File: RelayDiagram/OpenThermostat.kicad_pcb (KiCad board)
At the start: 2 copper layers, 9 parts, among them J1 Barrel_Jack_Switch, J2 Conn_01x15_Female, J3 Conn_01x15_Female, J4 Conn_01x08_Female, J5 Conn_01x11_Female, U1 R-78E3.3-1.0, U2 34.81-9024, U3 34.81-9024, U4 34.81-9024

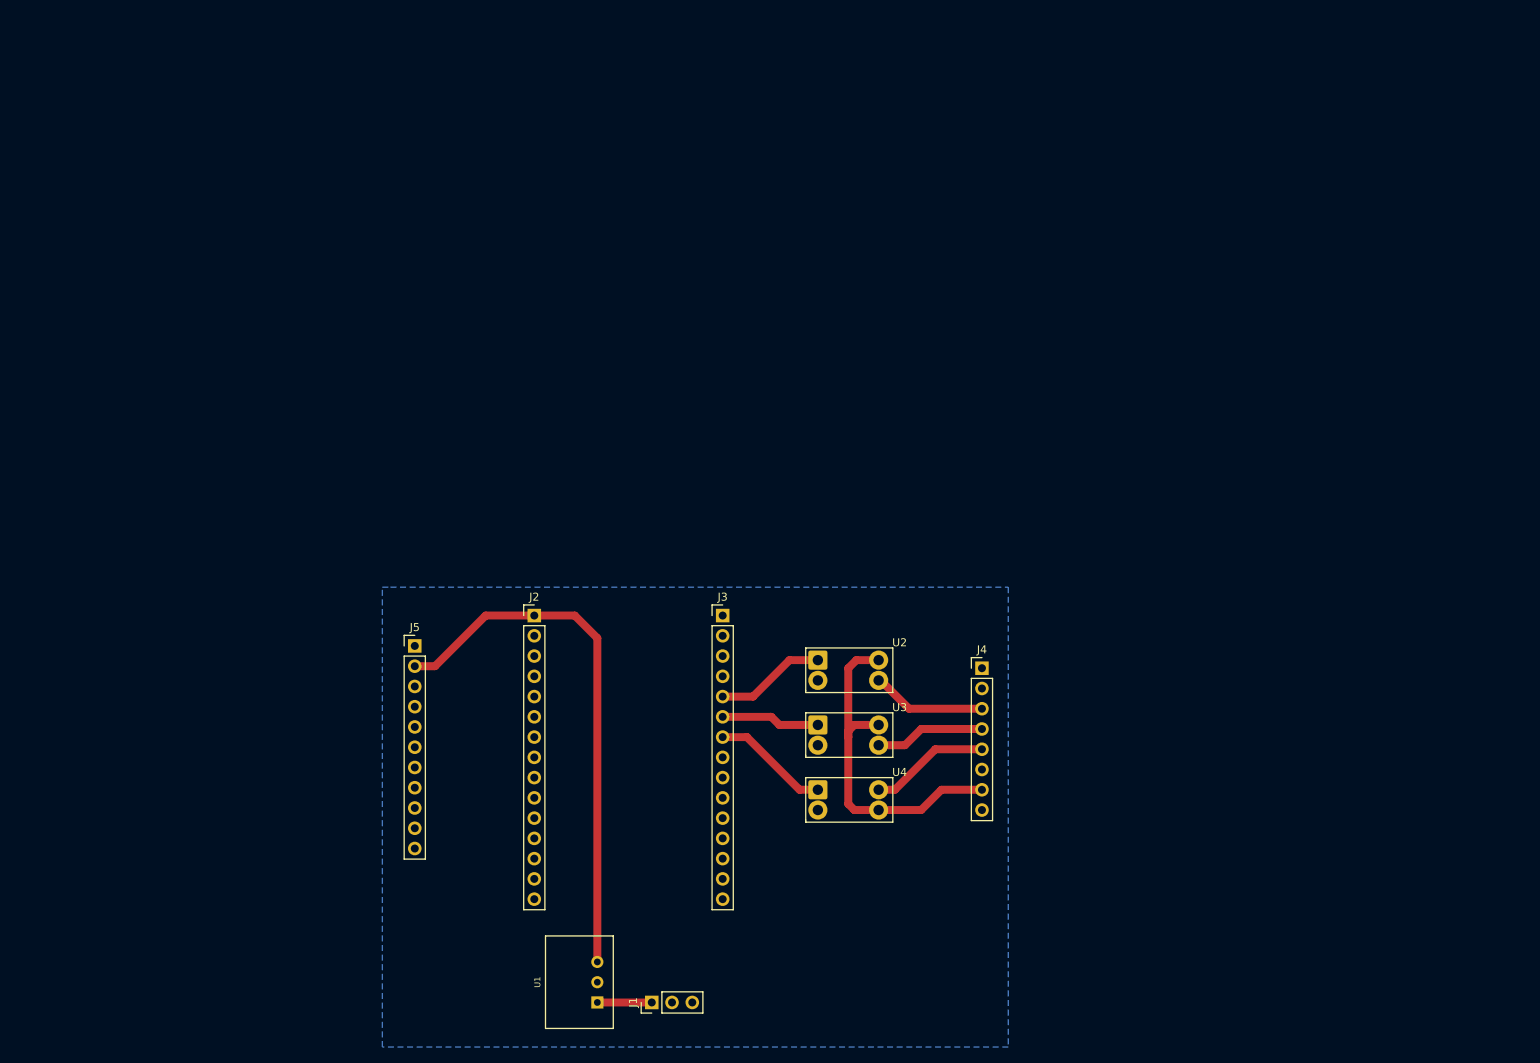
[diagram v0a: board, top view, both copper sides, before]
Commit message: Added footprints and started on PCB layout
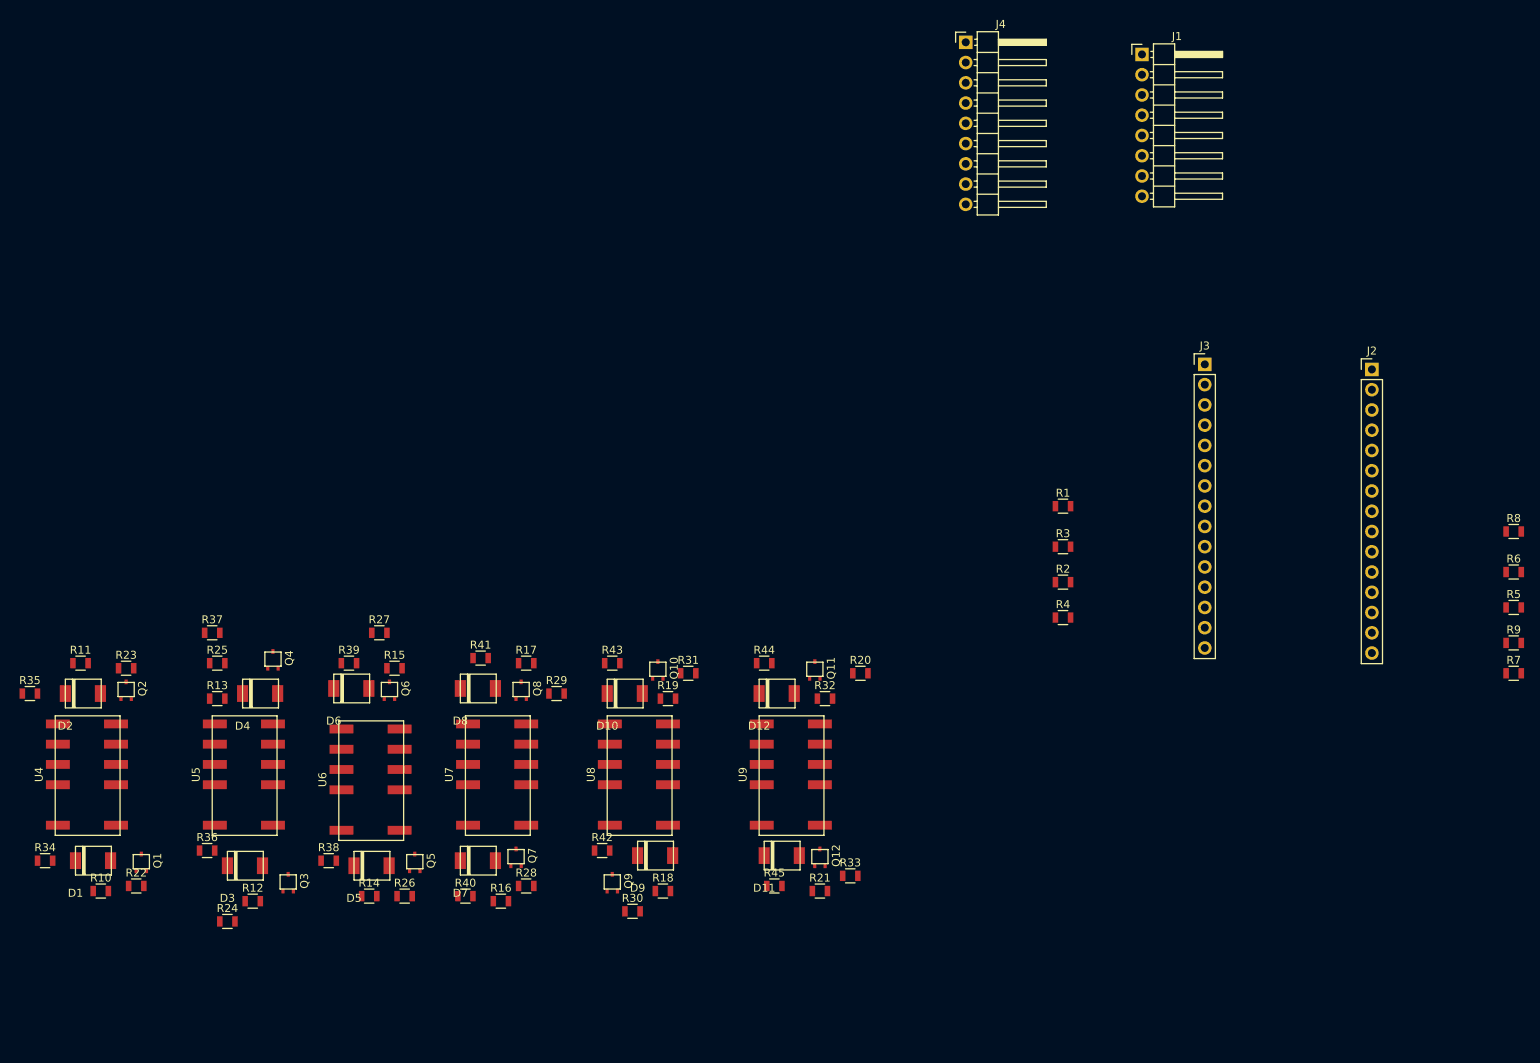
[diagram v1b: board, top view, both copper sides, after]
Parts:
- removed J5: Conn_01x11_Female, Pin_Headers:Pin_Header_Straight_1x11_Pitch2.54mm
- removed U1: R-78E3.3-1.0, solarcar-power:R-78E3.3-1.0
- removed U2, U3: 34.81-9024, OptoDevice:Placeholder
- added D1: D, SeniorDesign:SOD-128-Diode, F.Cu at (75.6, 87.6)
- added D10: D, SeniorDesign:SOD-128-Diode, F.Cu at (142.2, 66.7)
- added D11: D, SeniorDesign:SOD-128-Diode, F.Cu at (161.9, 87.0)
- added D12: D, SeniorDesign:SOD-128-Diode, F.Cu at (161.3, 66.7)
- added D2: D, SeniorDesign:SOD-128-Diode, F.Cu at (74.3, 66.7)
- added D3: D, SeniorDesign:SOD-128-Diode, F.Cu at (94.6, 88.3)
- added D4: D, SeniorDesign:SOD-128-Diode, F.Cu at (96.5, 66.7)
- added D5: D, SeniorDesign:SOD-128-Diode, F.Cu at (110.5, 88.3)
- added D6: D, SeniorDesign:SOD-128-Diode, F.Cu at (108.0, 66.0)
- added D7: D, SeniorDesign:SOD-128-Diode, F.Cu at (123.8, 87.6)
- added D8: D, SeniorDesign:SOD-128-Diode, F.Cu at (123.8, 66.0)
- added D9: D, SeniorDesign:SOD-128-Diode, F.Cu at (146.1, 87.0)
- added Q1: Q_NMOS_DGS, SeniorDesign:MCH3484-N-Channel-Mosfet, F.Cu at (83.8, 88.9)
- added Q10: Q_NMOS_DGS, SeniorDesign:MCH3484-N-Channel-Mosfet, F.Cu at (148.6, 64.8)
- added Q11: Q_NMOS_DGS, SeniorDesign:MCH3484-N-Channel-Mosfet, F.Cu at (168.3, 64.8)
- added Q12: Q_NMOS_DGS, SeniorDesign:MCH3484-N-Channel-Mosfet, F.Cu at (168.9, 88.3)
- added Q2: Q_NMOS_DGS, SeniorDesign:MCH3484-N-Channel-Mosfet, F.Cu at (81.9, 67.3)
- added Q3: Q_NMOS_DGS, SeniorDesign:MCH3484-N-Channel-Mosfet, F.Cu at (102.2, 91.4)
- added Q4: Q_NMOS_DGS, SeniorDesign:MCH3484-N-Channel-Mosfet, F.Cu at (100.3, 63.5)
- added Q5: Q_NMOS_DGS, SeniorDesign:MCH3484-N-Channel-Mosfet, F.Cu at (118.1, 88.9)
- added Q6: Q_NMOS_DGS, SeniorDesign:MCH3484-N-Channel-Mosfet, F.Cu at (114.9, 67.3)
- added Q7: Q_NMOS_DGS, SeniorDesign:MCH3484-N-Channel-Mosfet, F.Cu at (130.8, 88.3)
- added Q8: Q_NMOS_DGS, SeniorDesign:MCH3484-N-Channel-Mosfet, F.Cu at (131.4, 67.3)
- added Q9: Q_NMOS_DGS, SeniorDesign:MCH3484-N-Channel-Mosfet, F.Cu at (142.9, 91.4)
- added R1: 10k, Resistors_SMD:R_0805, F.Cu at (199.4, 43.2)
- added R10: 100, Resistors_SMD:R_0805, F.Cu at (78.7, 91.4)
- added R11: 100, Resistors_SMD:R_0805, F.Cu at (76.2, 62.9)
- added R12: 100, Resistors_SMD:R_0805, F.Cu at (97.8, 92.7)
- added R13: 100, Resistors_SMD:R_0805, F.Cu at (93.3, 67.3)
- added R14: 100, Resistors_SMD:R_0805, F.Cu at (112.4, 92.1)
- added R15: 100, Resistors_SMD:R_0805, F.Cu at (115.6, 63.5)
- added R16: 100, Resistors_SMD:R_0805, F.Cu at (128.9, 92.7)
- added R17: 100, Resistors_SMD:R_0805, F.Cu at (132.1, 62.9)
- added R18: 100, Resistors_SMD:R_0805, F.Cu at (149.2, 91.4)
- added R19: 100, Resistors_SMD:R_0805, F.Cu at (149.9, 67.3)
- added R2: 10k, Resistors_SMD:R_0805, F.Cu at (199.4, 52.7)
- added R20: 100, Resistors_SMD:R_0805, F.Cu at (174.0, 64.1)
- added R21: 100, Resistors_SMD:R_0805, F.Cu at (168.9, 91.4)
- added R22: 1M, Resistors_SMD:R_0805, F.Cu at (83.2, 90.8)
- added R23: 1M, Resistors_SMD:R_0805, F.Cu at (81.9, 63.5)
- added R24: 1M, Resistors_SMD:R_0805, F.Cu at (94.6, 95.2)
- added R25: 1M, Resistors_SMD:R_0805, F.Cu at (93.3, 62.9)
- added R26: 1M, Resistors_SMD:R_0805, F.Cu at (116.8, 92.1)
- added R27: 1M, Resistors_SMD:R_0805, F.Cu at (113.7, 59.1)
- added R28: 1M, Resistors_SMD:R_0805, F.Cu at (132.1, 90.8)
- added R29: 1M, Resistors_SMD:R_0805, F.Cu at (135.9, 66.7)
- added R3: 10k, Resistors_SMD:R_0805, F.Cu at (199.4, 48.3)
- added R30: 1M, Resistors_SMD:R_0805, F.Cu at (145.4, 94.0)
- added R31: 1M, Resistors_SMD:R_0805, F.Cu at (152.4, 64.1)
- added R32: 1M, Resistors_SMD:R_0805, F.Cu at (169.5, 67.3)
- added R33: 1M, Resistors_SMD:R_0805, F.Cu at (172.7, 89.5)
- added R34: 100, Resistors_SMD:R_0805, F.Cu at (71.8, 87.6)
- added R35: 100, Resistors_SMD:R_0805, F.Cu at (69.8, 66.7)
- added R36: 100, Resistors_SMD:R_0805, F.Cu at (92.1, 86.4)
- added R37: 100, Resistors_SMD:R_0805, F.Cu at (92.7, 59.1)
- added R38: 100, Resistors_SMD:R_0805, F.Cu at (107.3, 87.6)
- added R39: 100, Resistors_SMD:R_0805, F.Cu at (109.9, 62.9)
- added R4: 5k, Resistors_SMD:R_0805, F.Cu at (199.4, 57.1)
- added R40: 100, Resistors_SMD:R_0805, F.Cu at (124.5, 92.1)
- added R41: 100, Resistors_SMD:R_0805, F.Cu at (126.4, 62.2)
- added R42: 100, Resistors_SMD:R_0805, F.Cu at (141.6, 86.4)
- added R43: 100, Resistors_SMD:R_0805, F.Cu at (142.9, 62.9)
- added R44: 100, Resistors_SMD:R_0805, F.Cu at (161.9, 62.9)
- added R45: 100, Resistors_SMD:R_0805, F.Cu at (163.2, 90.8)
- added R5: 1M, Resistors_SMD:R_0805, F.Cu at (255.9, 55.9)
- added R6: 1M, Resistors_SMD:R_0805, F.Cu at (255.9, 51.4)
- added R7: 1M, Resistors_SMD:R_0805, F.Cu at (255.9, 64.1)
- added R8: 1M, Resistors_SMD:R_0805, F.Cu at (255.9, 46.4)
- added R9: 1M, Resistors_SMD:R_0805, F.Cu at (255.9, 60.3)
- added U5: EE2-3TNU-L_DPDT_Relay, SeniorDesign:EE2-5V-Relay, F.Cu at (100.3, 83.2)
- added U6: EE2-3TNU-L_DPDT_Relay, SeniorDesign:EE2-5V-Relay, F.Cu at (116.2, 83.8)
- added U7: EE2-3TNU-L_DPDT_Relay, SeniorDesign:EE2-5V-Relay, F.Cu at (132.1, 83.2)
- added U8: EE2-3TNU-L_DPDT_Relay, SeniorDesign:EE2-5V-Relay, F.Cu at (149.9, 83.2)
- added U9: EE2-3TNU-L_DPDT_Relay, SeniorDesign:EE2-5V-Relay, F.Cu at (168.9, 83.2)
- J1: value Barrel_Jack_Switch -> Conn_01x08_Female; footprint Pin_Headers:Pin_Header_Straight_1x03_Pitch2.54mm -> Pin_Headers:Pin_Header_Angled_1x08_Pitch2.54mm
- J4: value Conn_01x08_Female -> Conn_01x09_Female; footprint Pin_Headers:Pin_Header_Straight_1x08_Pitch2.54mm -> Pin_Headers:Pin_Header_Angled_1x09_Pitch2.54mm
- U4: value 34.81-9024 -> EE2-3TNU-L_DPDT_Relay; footprint OptoDevice:Placeholder -> SeniorDesign:EE2-5V-Relay
- moved J1 133.8 mm to (209.3, -13.5), turned to 0 degrees
- moved J2 109.5 mm to (238.1, 26.0)
- moved U4 88.1 mm to (80.6, 83.2), turned to 90 degrees
- moved J4 78.5 mm to (187.2, -15.0)
- moved J3 68.2 mm to (217.2, 25.4)
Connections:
- J1 pad 2: GND -> Net-(J1-Pad2)
- J2 pad 1: +3V3 -> Net-(J2-Pad1)
- J2 pad 6: Net-(J2-Pad6) -> Net-(J2-Pad11)
- J2 pad 7: Net-(J2-Pad7) -> Net-(J2-Pad14)
- J3 pad 1: Net-(J3-Pad1) -> +5V
- J4 pad 1: Net-(J4-Pad1) -> /RC
- J4 pad 2: Net-(J4-Pad2) -> /R
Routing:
- net +3V3: track 67.3 -> 0.00 mm
- net Net-(J4-Pad7): track 44.3 -> 0.00 mm
- net Net-(J4-Pad5): track 15.1 -> 0.00 mm
- net Net-(J3-Pad7): track 14.7 -> 0.00 mm
- net Net-(J4-Pad3): track 14.4 -> 0.00 mm
- net Net-(J3-Pad5): track 13.8 -> 0.00 mm
- net Net-(J4-Pad4): track 13.8 -> 0.00 mm
- net Net-(J3-Pad6): track 12.4 -> 0.00 mm
- net Net-(J1-Pad1): track 6.83 -> 0.00 mm
- removed copper zone on B.Cu, net GND
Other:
- rule pad_to_mask_clearance: 0.2 -> 0

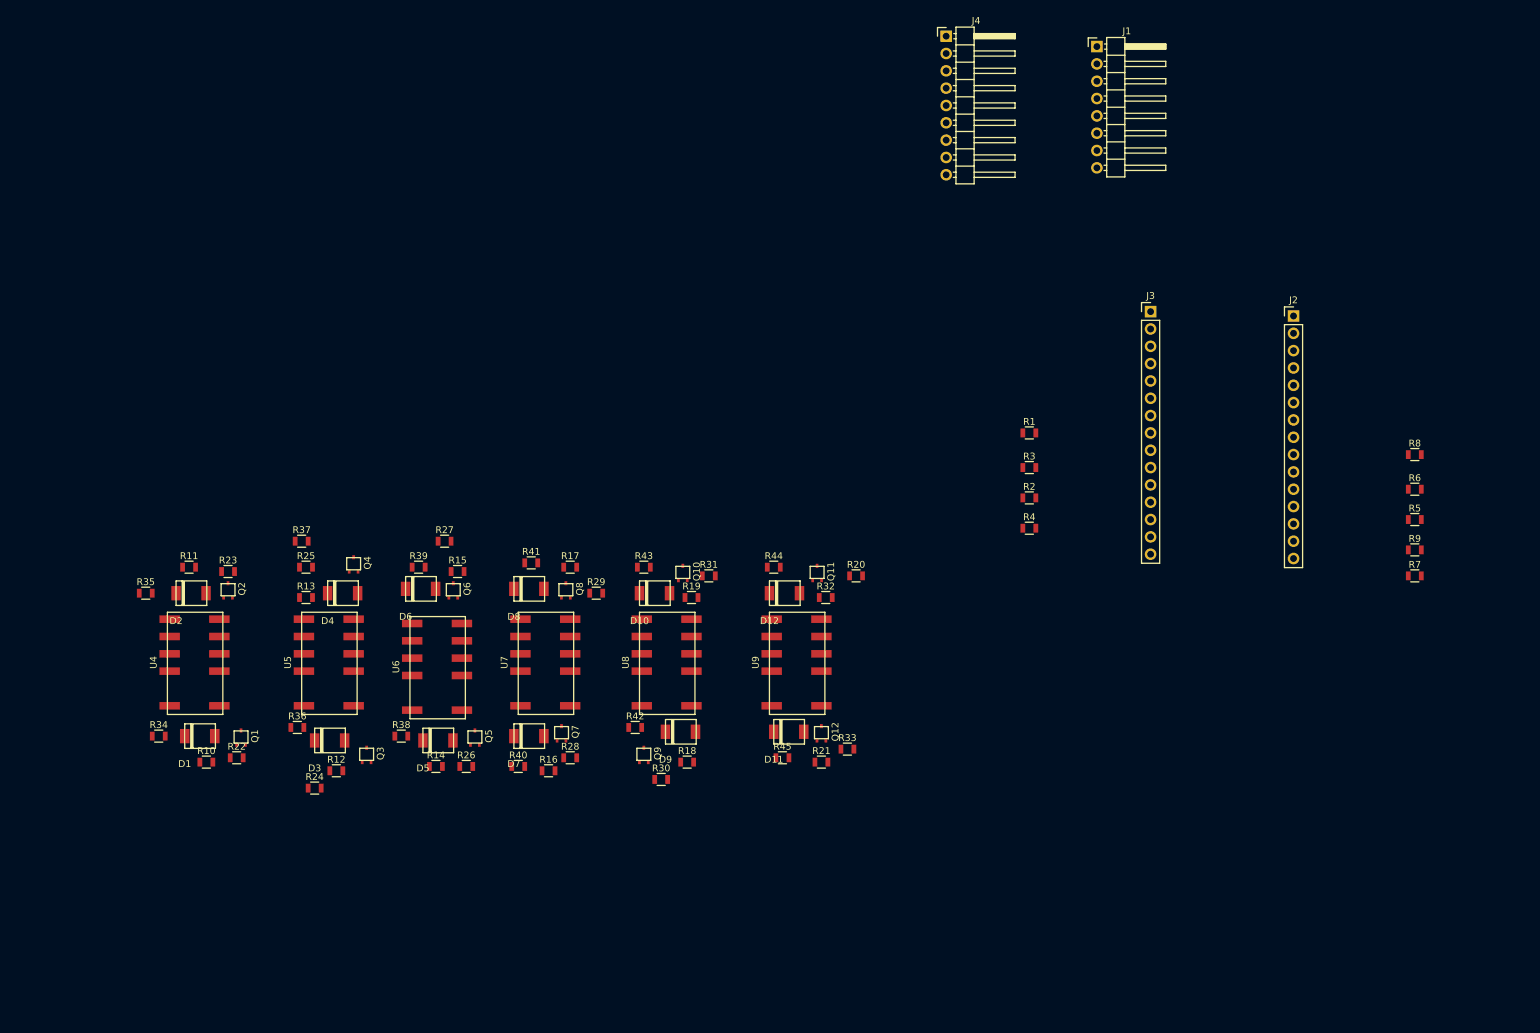
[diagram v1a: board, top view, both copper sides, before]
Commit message: Started PCB design with I/O Expander and Temp sensor, changed wires for I2c
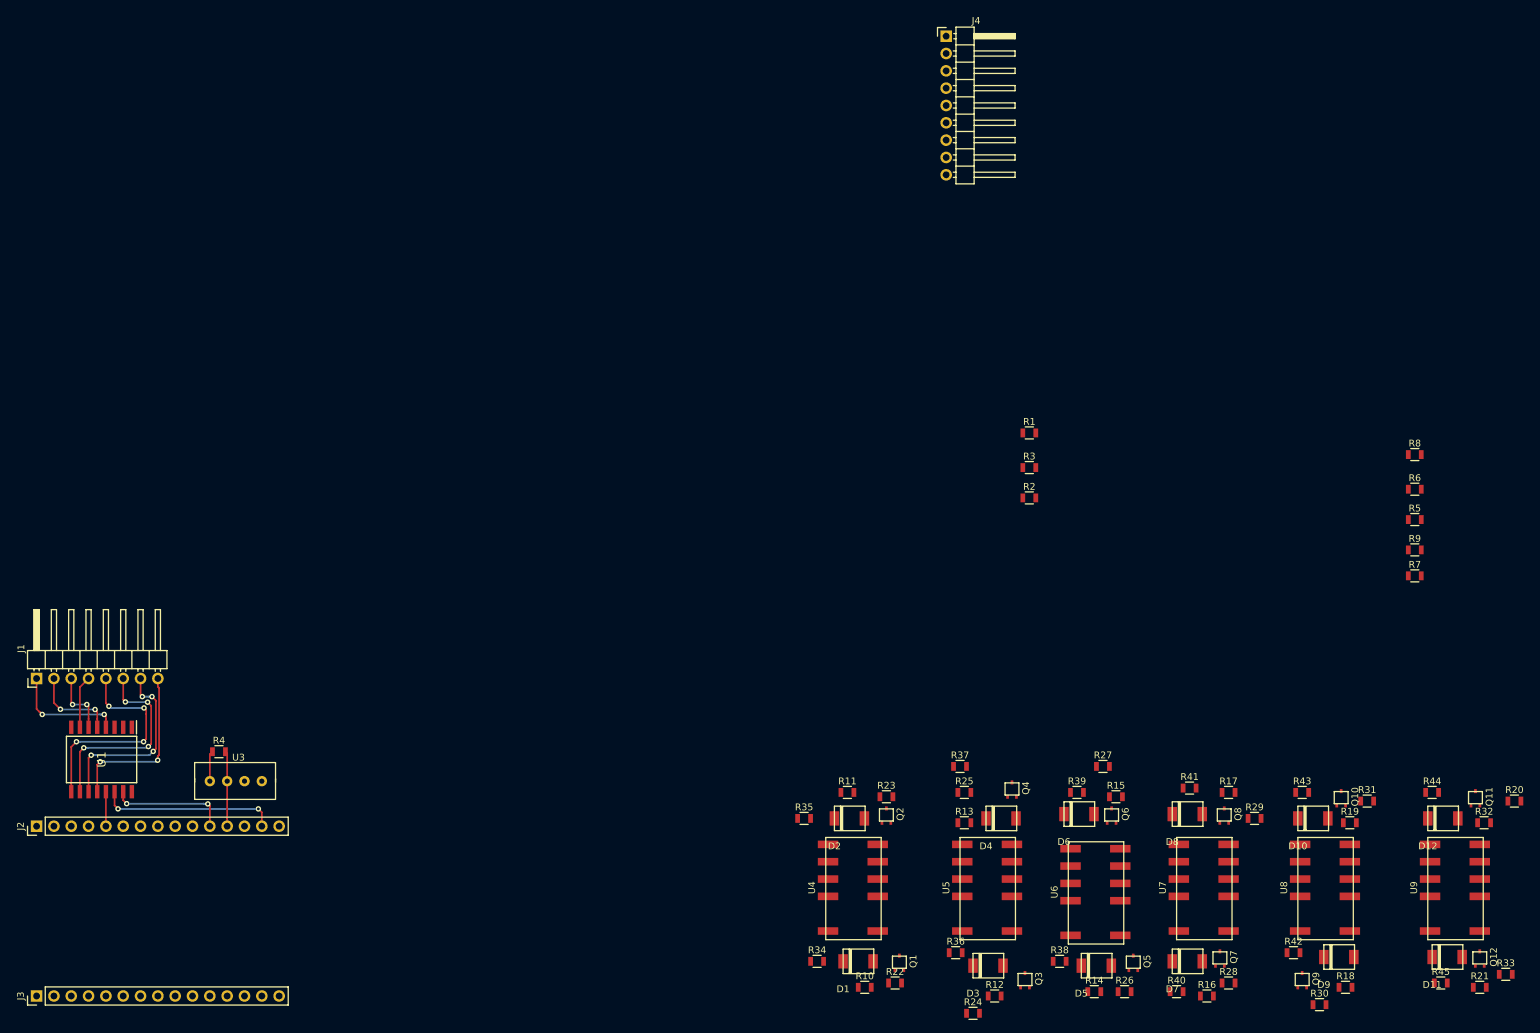
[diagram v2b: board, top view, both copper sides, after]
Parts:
- added U1: PCF8574, SeniorDesignLibrary:SOIC127P1030X265-16N, F.Cu at (63.4, 91.1)
- added U3: DHT11, SeniorDesignLibrary:DHT-11, F.Cu at (83.3, 94.2)
- moved J2 198.9 mm to (53.8, 100.8), turned to 90 degrees
- moved J3 191.7 mm to (53.8, 125.7), turned to 90 degrees
- moved J1 181.0 mm to (53.8, 79.2), turned to 90 degrees
- moved R4 123.2 mm to (80.6, 89.9)
- moved D1 102.0 mm to (172.1, 120.7)
- moved D12 102.0 mm to (257.8, 99.7)
- moved Q1 102.0 mm to (180.3, 121.9)
- moved Q10 102.0 mm to (245.1, 97.8)
- moved Q11 102.0 mm to (264.8, 97.8)
- moved Q12 102.0 mm to (265.4, 121.3)
- moved Q6 102.0 mm to (211.5, 100.3)
- moved Q7 102.0 mm to (227.3, 121.3)
- moved Q8 102.0 mm to (228.0, 100.3)
- moved Q9 102.0 mm to (239.4, 124.5)
- moved R13 102.0 mm to (189.9, 100.3)
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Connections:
- J2 pad 6: Net-(J2-Pad11) -> Net-(J2-Pad6)
- J2 pad 7: Net-(J2-Pad14) -> Net-(J2-Pad7)
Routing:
- net Net-(J1-Pad5): track 0.00 -> 32.2 mm, vias 0 -> 4
- net Net-(J1-Pad6): track 0.00 -> 29.9 mm, vias 0 -> 4
- net Net-(J1-Pad7): track 0.00 -> 27.4 mm, vias 0 -> 4
- net Net-(J2-Pad14): track 0.00 -> 26.0 mm, vias 0 -> 2
- net Net-(J1-Pad8): track 0.00 -> 25.2 mm, vias 0 -> 2
- net Net-(J2-Pad11): track 0.00 -> 17.3 mm, vias 0 -> 2
- net Net-(J1-Pad1): track 0.00 -> 16.7 mm, vias 0 -> 2
- net Net-(J1-Pad2): track 0.00 -> 12.7 mm, vias 0 -> 2
- net Net-(J2-Pad12): track 0.00 -> 11.0 mm
- net Net-(J1-Pad3): track 0.00 -> 9.43 mm, vias 0 -> 2
- net Net-(J1-Pad4): track 0.00 -> 7.68 mm
- net Net-(J2-Pad5): track 0.00 -> 5.05 mm
- net +5V: track 0.00 -> 4.48 mm
